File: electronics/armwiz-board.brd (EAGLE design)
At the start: 99.1 x 50.8 mm, 100 parts, among them IC3 SN74LVC1G74DCT, J1 MICRO-SDCARD-CONNECTOR-330006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, Q1 DMP2035U-7, Q2 DMP2035U-7, Q3 DMN2075U-7, Q4 DMN2075U-7, Q5 DMP2035U-7, U1 STM32F10XRXT6, U2 APX809, U3 MCP73831, U4 MIC5219-3.3V, X1 FH12-12S-1S

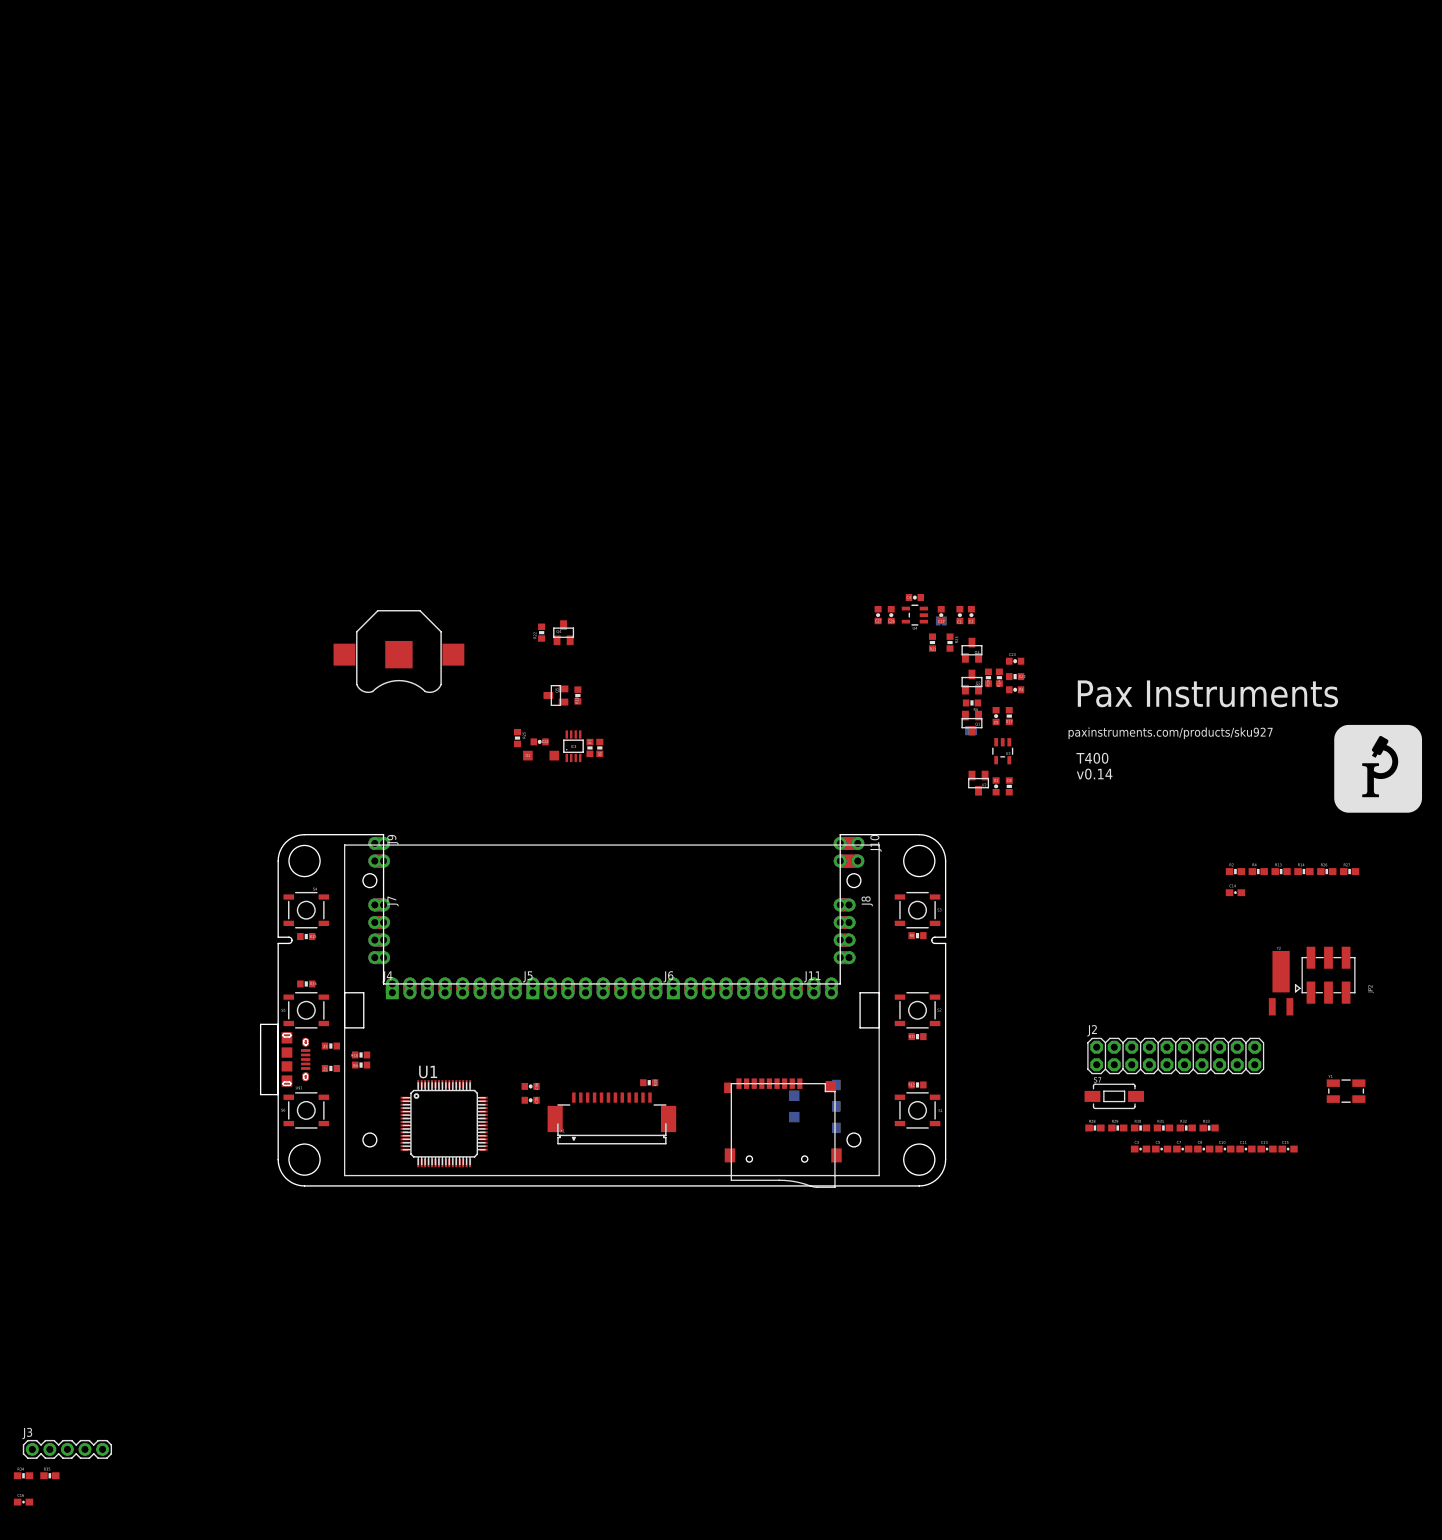
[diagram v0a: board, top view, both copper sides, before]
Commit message: Removed JTAG and ST-Link connectors. Added ARM Cortex Debug connector.
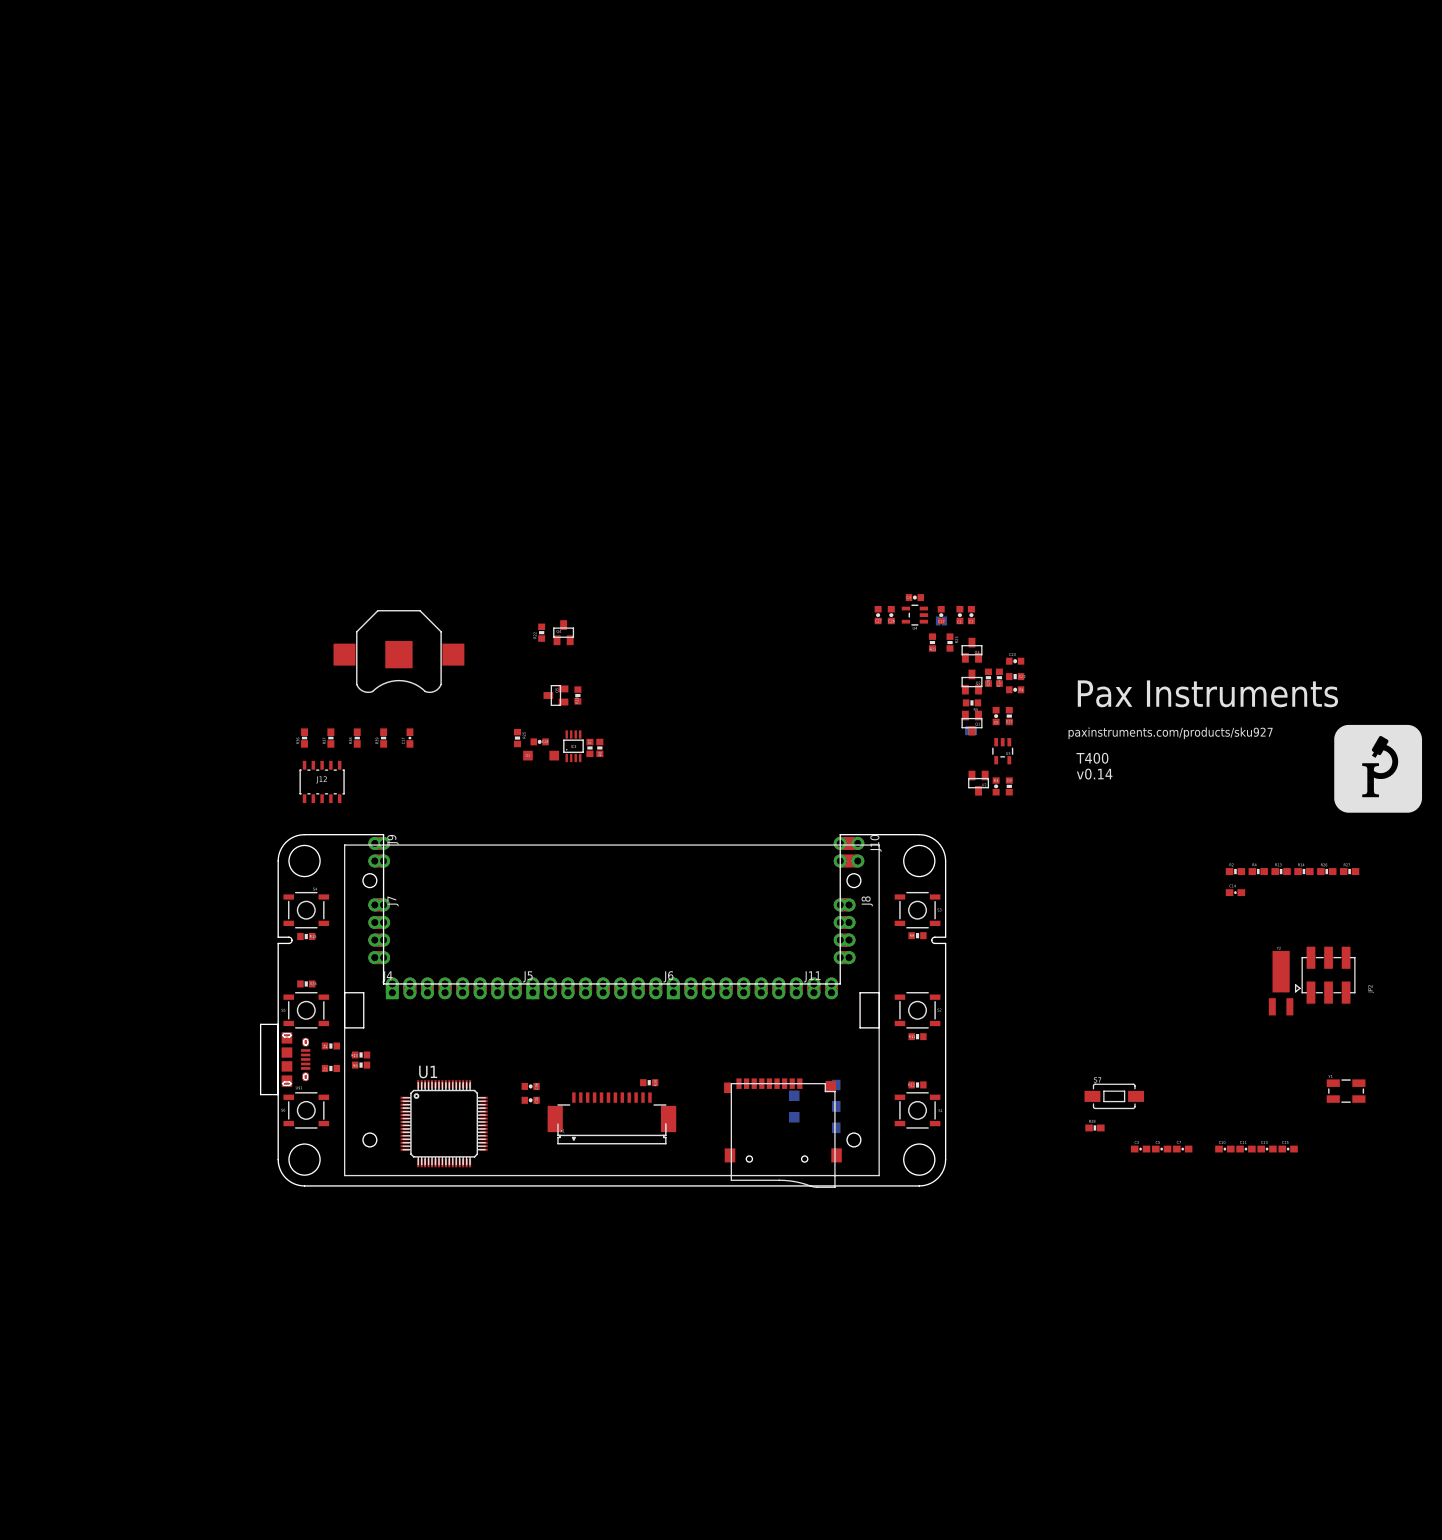
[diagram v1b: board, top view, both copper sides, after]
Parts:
- removed C16, C8: 0.1uF, SparkFun-Capacitors:0603-CAP
- removed J2: (no value), SparkFun-Connectors:2X10
- removed J3: (no value), SparkFun-Connectors:1X05
- removed R29, R30, R31, R32, R33, R34, R35: 10K, SparkFun-Resistors:0603-RES
- added C17: 0.1uF, SparkFun-Capacitors:0603-CAP
- added J12: CORTEX_DEBUGSMD, SparkFun-Connectors:SAMTECH_FTSH-105-01
- added R36, R37, R38, R39: 10K, SparkFun-Resistors:0603-RES
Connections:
- removed net 5V: J3.5
- removed net TCK: J2.9, J3.3, R33.1, R34.1, U1.49
- removed net TDO: J2.13, R32.1, U1.55
- removed net TMS: J2.7, J3.1, R31.1, R35.1, U1.46
- new net SWDCLK: J12.4, R37.2, U1.49
- new net SWDIO: J12.2, R36.1, U1.46
- new net SWO: J12.6, R38.2, U1.55
- net 3.3V: now also C17.2, J12.1, R36.2, R38.1, R39.1; no longer C16.2, C8.2, J2.1, J2.2, J3.4, R29.2, R30.2, R31.2, R32.2, R35.2
- net GND: now also C17.1, J12.3, J12.5, J12.9, R37.1; no longer C16.1, C8.1, J2.10, J2.12, J2.14, J2.16, J2.18, J2.20, J2.4, J2.6, J2.8, J3.2, R33.2, R34.2
- net NRST: now also J12.10; no longer J2.15
- net TDI: now also J12.8, R39.2; no longer J2.5, R30.1
- net TRST: no longer J2.3, R29.1
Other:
- board text added: "Cortex Debug"

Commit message: Readded the ST Link connection. I'll try to keep them both.
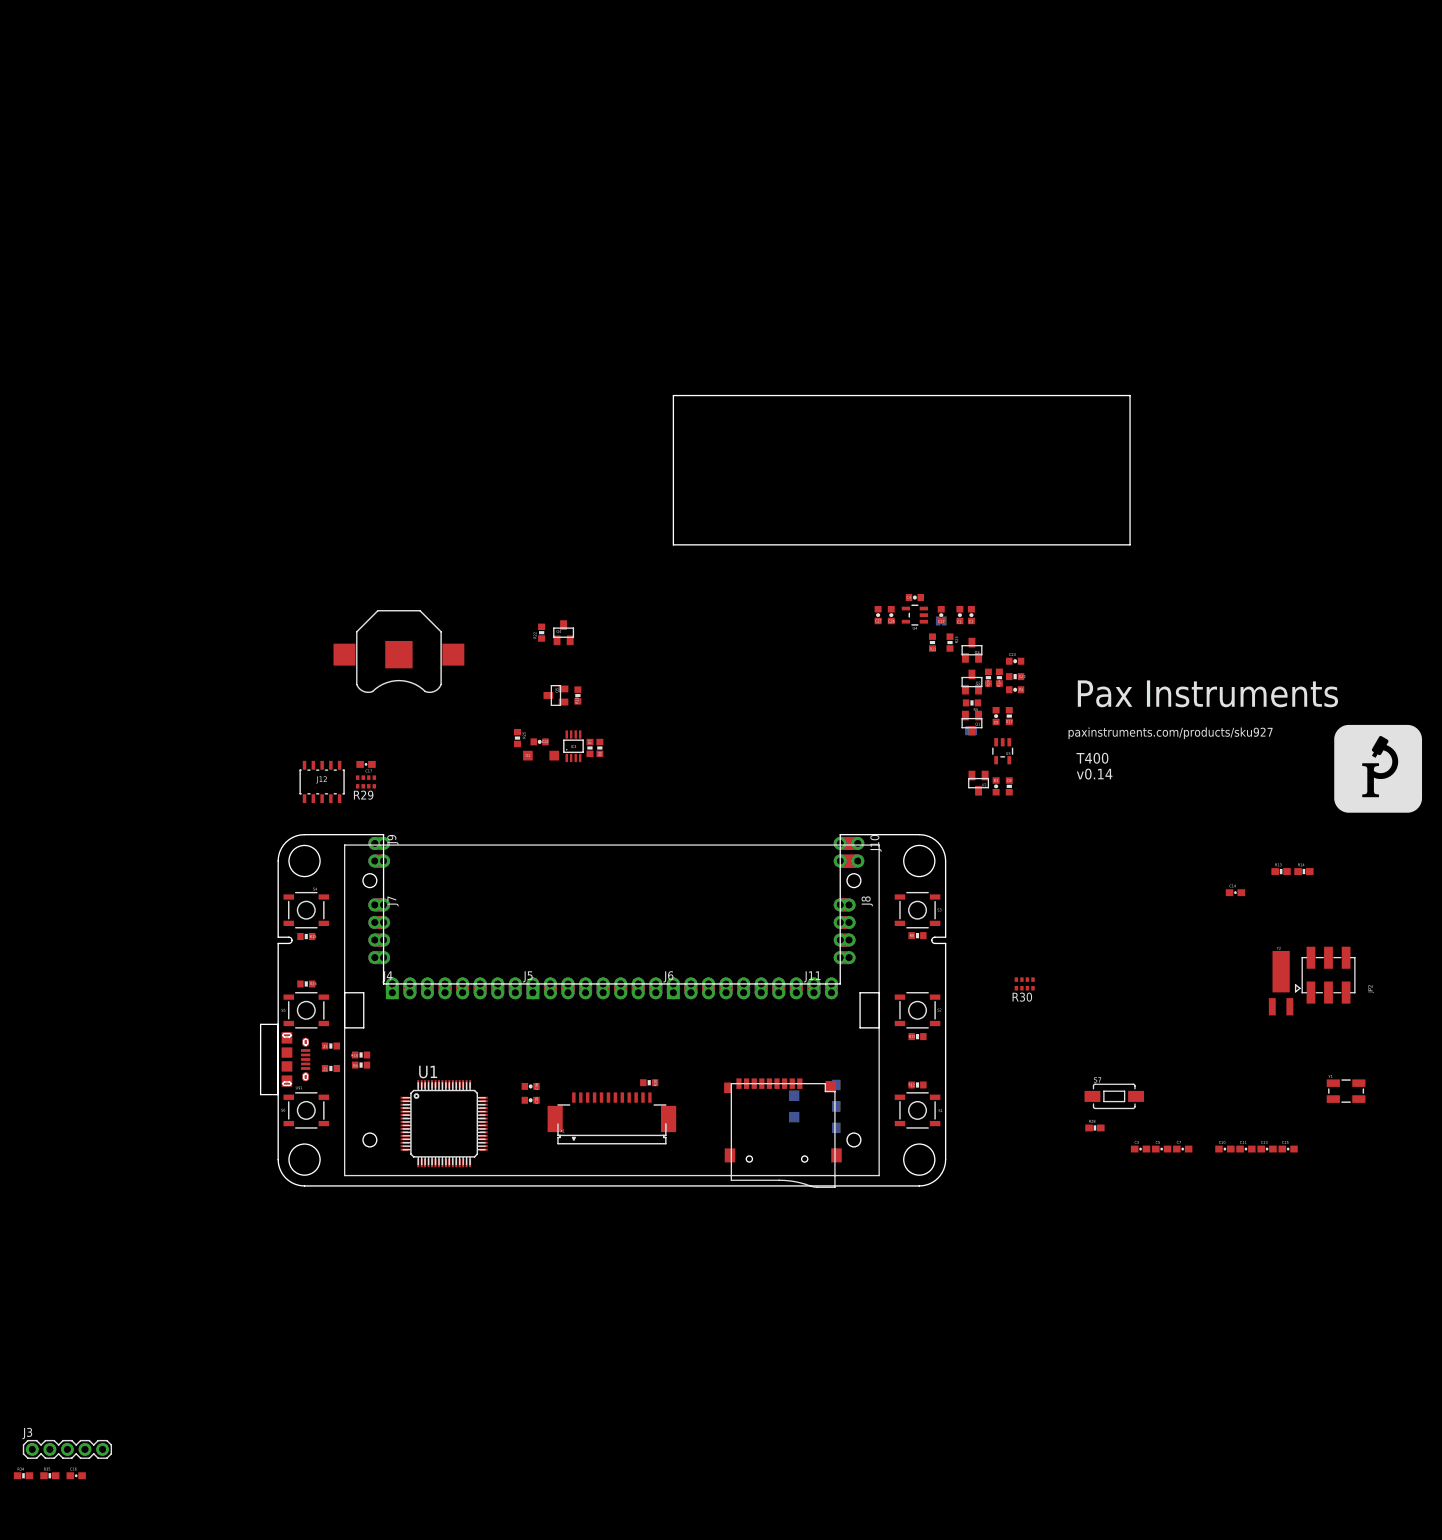
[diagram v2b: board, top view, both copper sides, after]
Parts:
- removed R2, R26, R27, R36, R37, R38, R39, R4: 10K, SparkFun-Resistors:0603-RES
- added C16: 0.1uF, SparkFun-Capacitors:0603-CAP
- added J3: (no value), SparkFun-Connectors:1X05
- added R29, R30: 10k, SparkFun-Passives:0603-ARV
- added R34, R35: 10K, SparkFun-Resistors:0603-RES
- moved C17 7.41 mm to (12.7, 61.0), turned to 180 degrees
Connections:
- new net 5V: J3.5
- net 3.3V: now also C16.2, J3.4, R29.6, R29.7, R29.8, R30.1, R30.2, R30.3, R30.4, R35.2; no longer R2.1, R26.1, R27.1, R36.2, R38.1, R39.1, R4.1
- net GND: now also C16.1, J3.2, R29.4, R34.2; no longer R37.1
- net SDIO_D0: now also R30.6; no longer R4.2
- net SDIO_D1: now also R30.5; no longer R2.2
- net SDIO_D2: now also R30.8; no longer R27.2
- net SDIO_D3: now also R30.7; no longer R26.2
- net SWDCLK: now also J3.3, R29.5, R34.1; no longer R37.2
- net SWDIO: now also J3.1, R29.1, R35.1; no longer R36.1
- net SWO: now also R29.2; no longer R38.2
- net TDI: now also R29.3; no longer R39.2
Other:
- board size 99.1 x 50.8 mm -> 125.7 x 114.3 mm

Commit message: Cleaned up the schematic. No electrical changes.
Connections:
- removed net N$13: U1.4, Y2.X2
- removed net N$14: U1.3, Y2.X1
- removed net N$31: R10.1, U$1.PIN$2, Z2.2
- removed net N$33: R9.1, U$1.PIN$3, Z1.2
- removed net N$35: U1.45
- removed net N$36: U1.44
- new net RTC1: U1.3, Y2.X2
- new net RTC2: U1.4, Y2.X1
- new net USB+: R9.2, U1.45
- new net USB-: R10.2, U1.44
- net 3.3V: no longer U1.1
- net D+: now also R9.1, U$1.PIN$3, Z1.2; no longer R9.2
- net D-: now also R10.1, U$1.PIN$2, Z2.2; no longer R10.2
- net RTC_BATT: now also U1.1
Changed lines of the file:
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@@
 <contactref element="U1" pad="19"/>
 <contactref element="U1" pad="13"/>
-<contactref element="U1" pad="1"/>
 <contactref element="JP2" pad="1"/>
 <contactref element="JP2" pad="2"/>
@@
 <wire x1="29.7" y1="12.75" x2="46.76" y2="12.775" width="0" layer="19" extent="1-1"/>
 <wire x1="20.25" y1="14.7" x2="29.7" y2="12.75" width="0" layer="19" extent="1-1"/>
-<wire x1="18.3" y1="12.75" x2="20.25" y2="14.7" width="0" layer="19" extent="1-1"/>
-<wire x1="18.3" y1="6.75" x2="18.3" y2="12.75" width="0" layer="19" extent="1-1"/>
+<wire x1="18.3" y1="6.75" x2="20.25" y2="14.7" width="0" layer="19" extent="1-1"/>
 <wire x1="21.25" y1="3.3" x2="18.3" y2="6.75" width="0" layer="19" extent="1-1"/>
 <wire x1="27.75" y1="3.3" x2="21.25" y2="3.3" width="0" layer="19" extent="1-1"/>
-<wire x1="3.214" y1="29.21" x2="18.3" y2="12.75" width="0" layer="19" extent="1-1"/>
+<wire x1="3.214" y1="29.21" x2="20.25" y2="14.7" width="0" layer="19" extent="1-1"/>
 <wire x1="3.214" y1="36.068" x2="3.214" y2="29.21" width="0" layer="19" extent="1-1"/>
 <wire x1="3.81" y1="56.007" x2="3.214" y2="36.068" width="0" layer="19" extent="1-1"/>
@@
 <wire x1="-30.06" y1="-41.91" x2="-33.02" y2="-38.1" width="0" layer="19" extent="1-1"/>
 </signal>
-<signal name="D-">
+<signal name="USB-">
 <contactref element="R10" pad="2"/>
-</signal>
-<signal name="D+">
+<contactref element="U1" pad="44"/>
+<wire x1="12.835625" y1="18.938" x2="29.7" y2="10.75" width="0" layer="19" extent="1-1"/>
+</signal>
+<signal name="USB+">
 <contactref element="R9" pad="2"/>
+<contactref element="U1" pad="45"/>
+<wire x1="12.835625" y1="17.47925" x2="29.7" y2="11.25" width="0" layer="19" extent="1-1"/>
 </signal>
 <signal name="MOSI">
@@
 <signal name="RTC_BATT">
 <contactref element="BAT1" pad="PWR@1"/>
+<contactref element="U1" pad="1"/>
+<wire x1="18.3" y1="12.75" x2="25.3365" y2="76.835" width="0" layer="19" extent="1-1"/>
 </signal>
 <signal name="N$3">
@@
 <wire x1="3.97" y1="19.588" x2="34.6075" y2="63.92" width="0" layer="19" extent="1-1"/>
 </signal>
-<signal name="N$31">
+<signal name="D-">
 <contactref element="U$1" pad="PIN$2"/>
 <contactref element="R10" pad="1"/>
@@
 <wire x1="3.97" y1="18.938" x2="6.77" y2="20.238" width="0" layer="19" extent="1-1"/>
 </signal>
-<signal name="N$33">
+<signal name="D+">
 <contactref element="U$1" pad="PIN$3"/>
 <contactref element="R9" pad="1"/>
@@
 <wire x1="18.3" y1="10.75" x2="129.96" y2="5.334" width="0" layer="19" extent="1-1"/>
 </signal>
-<signal name="N$13">
+<signal name="RTC2">
 <contactref element="U1" pad="4"/>
+<contactref element="Y2" pad="X1"/>
+<wire x1="18.3" y1="11.25" x2="143.764" y2="25.908" width="0" layer="19" extent="1-1"/>
+</signal>
+<signal name="RTC1">
+<contactref element="U1" pad="3"/>
 <contactref element="Y2" pad="X2"/>
-<wire x1="146.304" y1="25.908" x2="18.3" y2="11.25" width="0" layer="19" extent="1-1"/>
-</signal>
-<signal name="N$14">
-<contactref element="U1" pad="3"/>
-<contactref element="Y2" pad="X1"/>
-<wire x1="143.764" y1="25.908" x2="18.3" y2="11.75" width="0" layer="19" extent="1-1"/>
+<wire x1="18.3" y1="11.75" x2="146.304" y2="25.908" width="0" layer="19" extent="1-1"/>
 </signal>
 <signal name="BOOT1">
@@
 <wire x1="6.35" y1="60.833" x2="24.75" y2="14.7" width="0" layer="19" extent="1-1"/>
 </signal>
-<signal name="N$35">
-<contactref element="U1" pad="45"/>
-</signal>
-<signal name="N$36">
-<contactref element="U1" pad="44"/>
-</signal>
 <signal name="RX1">

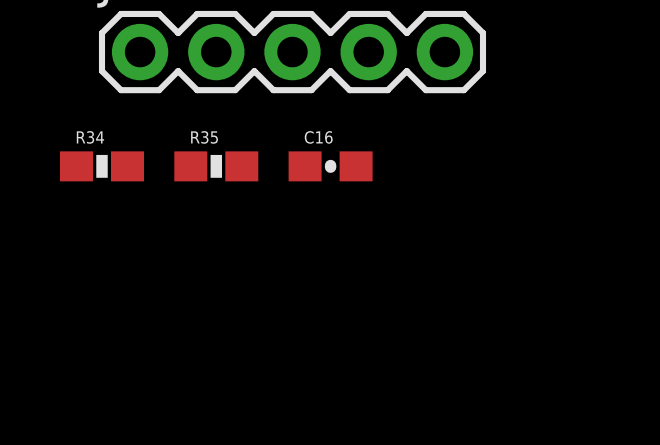
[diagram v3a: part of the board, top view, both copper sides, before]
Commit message: Copied labels for all the pins that need to be connected to the MCU.
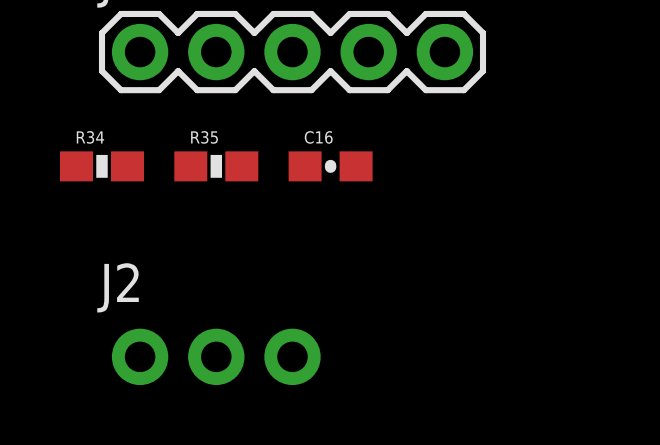
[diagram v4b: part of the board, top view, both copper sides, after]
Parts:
- added J2: (no value), SparkFun-Connectors:1X03_NO_SILK
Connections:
- net GND: now also J2.3
- net RX1: now also J2.1
- net TX1: now also J2.2
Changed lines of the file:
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@@
 <attribute name="PROD_ID" value="CAP-08604" x="-36.83" y="-49.53" size="1.778" layer="27" display="off"/>
 </element>
+<element name="J2" library="SparkFun-Connectors" package="1X03_NO_SILK" value="" x="-35.56" y="-48.26"/>
 </elements>
 <signals>
@@
 <contactref element="C16" pad="1"/>
 <contactref element="R34" pad="2"/>
+<contactref element="J2" pad="3"/>
 <wire x1="154.432" y1="27.96" x2="154.432" y2="33" width="0" layer="19" extent="1-1"/>
 <wire x1="137.58" y1="42.418" x2="154.432" y2="33" width="0" layer="19" extent="1-1"/>
@@
 <wire x1="-35.98" y1="-41.91" x2="-33.02" y2="-38.1" width="0" layer="19" extent="1-1"/>
 <wire x1="-30.06" y1="-41.91" x2="-33.02" y2="-38.1" width="0" layer="19" extent="1-1"/>
+<wire x1="-30.48" y1="-48.26" x2="-30.06" y2="-41.91" width="0" layer="19" extent="1-1"/>
 </signal>
 <signal name="USB-">
@@
 <signal name="RX1">
 <contactref element="U1" pad="43"/>
+<contactref element="J2" pad="1"/>
+<wire x1="29.7" y1="10.25" x2="-35.56" y2="-48.26" width="0" layer="19" extent="1-1"/>
 </signal>
 <signal name="TX1">
 <contactref element="U1" pad="42"/>
+<contactref element="J2" pad="2"/>
+<wire x1="29.7" y1="9.75" x2="-33.02" y2="-48.26" width="0" layer="19" extent="1-1"/>
 </signal>
 <signal name="N$40">
